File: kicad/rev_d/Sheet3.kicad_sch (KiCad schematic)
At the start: 106 parts, among them U1 74HCT1G04, X10 ST-214C, X14 AAFP/AC97 audio, X16 PLB1-4I, X17 PLB1-4I, X18 PLB1-4I, X20 PLB1-4I

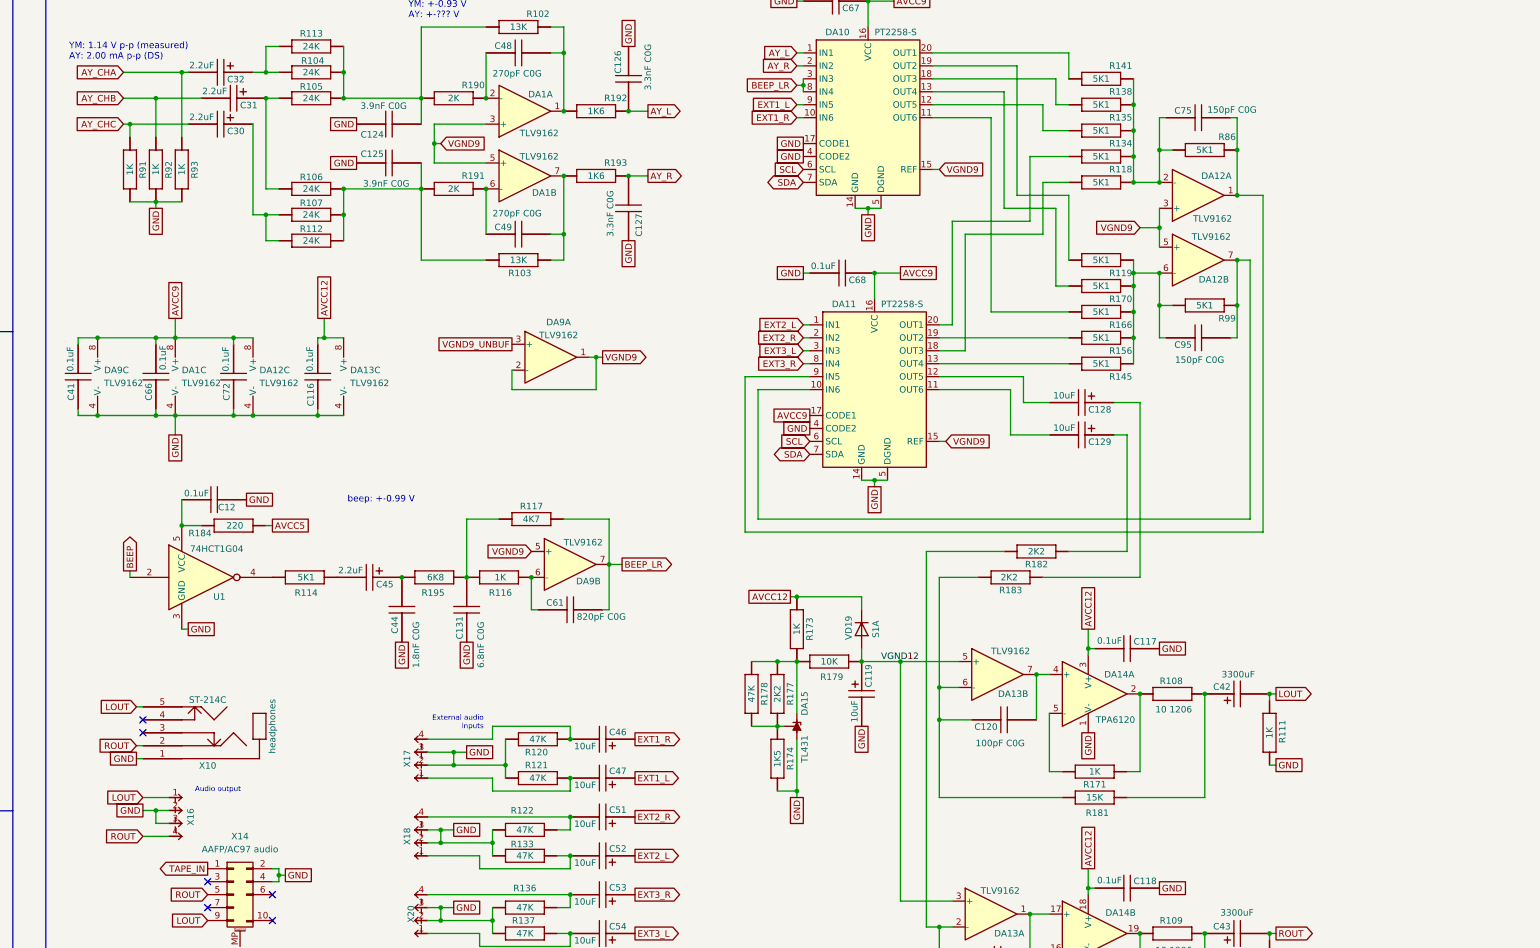
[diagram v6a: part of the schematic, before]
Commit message: pentevo: rev D: change 3.5mm and pins to be line output, keep AC97 as headphones
git-svn-id: svn://localhost/local-pentevo@1266 c6c76956-fad2-4150-a3a9-ea0a427205ba
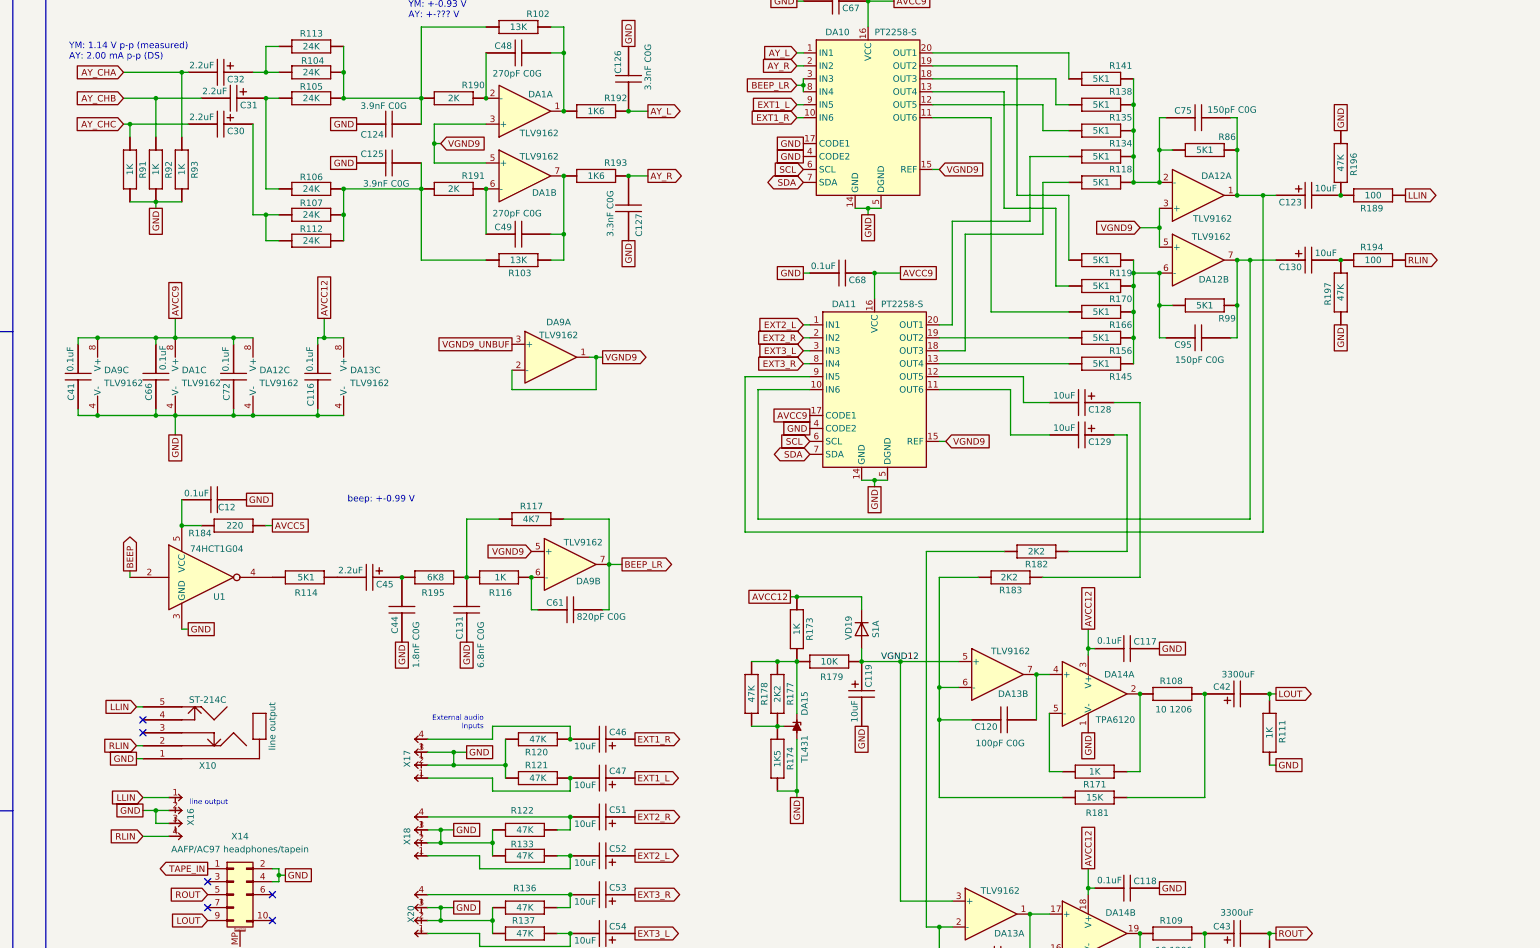
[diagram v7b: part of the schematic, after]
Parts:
- added C123, C130: 10uF, EC-CHIP, symbol eva-altium-import:Sheet2_0_ECAPCHIP
- added R189, R194: 100, R-CHIP, symbol eva-altium-import:Sheet2_0_RESCHIP
- added R196, R197: 47K, R-CHIP, symbol eva-altium-import:Sheet2_0_RESCHIP
- X10: ALTIUM_VALUE headphones -> line output
- X14: value AAFP/AC97 audio -> AAFP/AC97 headphones/tapein
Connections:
- net GND: now also R196.2 (i/o1), R197.1 (i/o)
- net LOUT: no longer X10.5, X16.1 (I/O1)
- net ROUT: no longer X10.2, X16.4 (I/O4)
- net at C95.2, DA11.10 (IN6), DA12.7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: now also C130.1
- net at C75.2, DA11.9 (IN5), DA12.1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: now also C123.1
- new net: C123.2, R189.1 (i/o), R196.1 (i/o)
- new net: C130.2, R194.1 (i/o), R197.2 (i/o1)
- new net LLIN: R189.2 (i/o1), X10.5, X16.1 (I/O1)
- new net RLIN: R194.2 (i/o1), X10.2, X16.4 (I/O4)

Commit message: pentevo: rev D: video output: make new sheet for video outputs
git-svn-id: svn://localhost/local-pentevo@1274 c6c76956-fad2-4150-a3a9-ea0a427205ba
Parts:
- renumbered U1 to D31
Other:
- note added: "Title: Analog audio"
- note removed: "Title"
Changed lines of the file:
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@@
 		)
 	)
-	(text "Title"
+	(text "Title: Analog audio"
 		(exclude_from_sim no)
 		(at 423.89 338.16 0)
@@
 		(pin "3"
 		)
-		(instances
-			(project ""
-				(path "/ab605654-a730-497b-9e09-9b351f74b935/d12fc3f7-914a-41f9-b933-632d1b3e89f3"
-					(reference "DA15")
-					(unit 1)
-				)
-			)
-		)
 	)
 	(symbol
@@
 		(pin "3"
 		)
-		(instances
-			(project ""
-				(path "/ab605654-a730-497b-9e09-9b351f74b935/d12fc3f7-914a-41f9-b933-632d1b3e89f3"
-					(reference "DA1")
-					(unit 2)
-				)
-			)
-		)
 	)
 	(symbol
@@
 		(pin "7"
 		)
-		(instances
-			(project ""
-				(path "/ab605654-a730-497b-9e09-9b351f74b935/d12fc3f7-914a-41f9-b933-632d1b3e89f3"
-					(reference "DA12")
-					(unit 3)
-				)
-			)
-		)
 	)
 	(symbol
@@
 		(on_board yes)
 		(dnp no)
-		(property "Reference" "U1"
+		(property "Reference" "D31"
 			(at 56.896 153.67 0)
 			(effects
@@
 			(project "eva"
 				(path "/ab605654-a730-497b-9e09-9b351f74b935/d12fc3f7-914a-41f9-b933-632d1b3e89f3"
-					(reference "U1")
+					(reference "D31")
 					(unit 1)
 				)
@@
 		(pin "3"
 		)
-		(instances
-			(project ""
-				(path "/ab605654-a730-497b-9e09-9b351f74b935/d12fc3f7-914a-41f9-b933-632d1b3e89f3"
-					(reference "DA1")
-					(unit 3)
-				)
-			)
-		)
 	)
 	(symbol
@@
 		(pin "2"
 		)
-		(instances
-			(project ""
-				(path "/ab605654-a730-497b-9e09-9b351f74b935/d12fc3f7-914a-41f9-b933-632d1b3e89f3"
-					(reference "DA9")
-					(unit 1)
-				)
-			)
-		)
 	)
 	(symbol
@@
 		(pin "16"
 		)
-		(instances
-			(project ""
-				(path "/ab605654-a730-497b-9e09-9b351f74b935/d12fc3f7-914a-41f9-b933-632d1b3e89f3"
-					(reference "DA14")
-					(unit 2)
-				)
-			)
-		)
 	)
 	(symbol
@@
 		(pin "2"
 		)
-		(instances
-			(project ""
-				(path "/ab605654-a730-497b-9e09-9b351f74b935/d12fc3f7-914a-41f9-b933-632d1b3e89f3"
-					(reference "DA9")
-					(unit 3)
-				)
-			)
-		)
 	)
 	(symbol
@@
 		(pin "2"
 		)
-		(instances
-			(project ""
-				(path "/ab605654-a730-497b-9e09-9b351f74b935/d12fc3f7-914a-41f9-b933-632d1b3e89f3"
-					(reference "DA9")
-					(unit 2)
-				)
-			)
-		)
 	)
 	(symbol
@@
 		(pin "5"
 		)
-		(instances
-			(project ""
-				(path "/ab605654-a730-497b-9e09-9b351f74b935/d12fc3f7-914a-41f9-b933-632d1b3e89f3"
-					(reference "DA10")
-					(unit 1)
-				)
-			)
-		)
 	)
 	(symbol
@@
 		(pin "16"
 		)
-		(instances
-			(project ""
-				(path "/ab605654-a730-497b-9e09-9b351f74b935/d12fc3f7-914a-41f9-b933-632d1b3e89f3"
-					(reference "DA14")
-					(unit 1)
-				)
-			)
-		)
 	)
